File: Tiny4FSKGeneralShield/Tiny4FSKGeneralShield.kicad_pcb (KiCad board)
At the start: 4 copper layers, 27.8 x 63.9 mm, 33 parts, among them J1 Micro_SD_Card, J10 Ext.IMU, J11 Ext.Photo, J12 Int.OLED, J15 Int.Pwr, J16 3v3 IO, J17 5V IO, J2 USB_C_Receptacle_USB2.0_14P, J3 TinyI2C, J4 TinyGPIO, J5 Ext.BME280, J6 TinySPI, J7 TinyPwr, J8 TinyUSB, J9 Ext.Pwr, U1 FXMA108, U3 TPS63060

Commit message: starting to get caught up
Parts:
- C3, C4, C5, C6: footprint Capacitor_SMD:C_0805_2012Metric -> Capacitor_SMD:C_0402_1005Metric
- C7, C8, C9: footprint Capacitor_SMD:C_0805_2012Metric -> Capacitor_SMD:C_0603_1608Metric
- J1: footprint Connector_Card:microSD_HC_Hirose_DM3D-SF -> TF-PUSH:TF-PUSH
- R1, R2: value 5k1 -> 5.1kR; footprint Resistor_SMD:R_0805_2012Metric -> Resistor_SMD:R_0402_1005Metric
- R3, R5: value 1k -> 1kR; footprint Resistor_SMD:R_0805_2012Metric -> Resistor_SMD:R_0402_1005Metric
- R4, R6: value 2k -> 2kR; footprint Resistor_SMD:R_0805_2012Metric -> Resistor_SMD:R_0402_1005Metric
- R7: footprint Resistor_SMD:R_0805_2012Metric -> Resistor_SMD:R_0402_1005Metric
- R9: value 111k -> 111kR
- moved J1 26.0 mm to (174.2, 72.5)
- moved R4 2.90 mm to (141.8, 96.6)
- moved C4 2.35 mm to (151.6, 100.3), turned to 0 degrees
- moved R3 1.94 mm to (140.4, 97.0)
- moved R7 1.74 mm to (150.2, 99.9)
- moved R6 1.31 mm to (141.8, 98.6)
- moved R9 0.98 mm to (151.0, 101.8)
- moved C3 0.75 mm to (151.7, 104.0)
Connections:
- J1 pad 9: Earth -> unconnected-(J1-DET-Pad9)
- J12 pad 1: +3.3V -> SDA
- J12 pad 2: Earth -> SCL
- J12 pad 3: SCL -> +3.3V
- J12 pad 4: SDA -> Earth
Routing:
- net Earth: track 17.7 -> 10.9 mm, vias 59 -> 51
- net SCK: track 80.0 -> 74.5 mm, vias 3 -> 2
- net Net-(U3-FB): track 9.87 -> 5.76 mm
- net MOSI: track 114.6 -> 110.7 mm, vias 1 -> 0
- net MISO: track 77.3 -> 74.0 mm, vias 3 -> 2
- net A1: track 66.5 -> 69.6 mm
- net SDA: track 83.8 -> 80.9 mm, vias 0 -> 1
- net A1_5: track 20.3 -> 17.9 mm, vias 1 -> 0
- net +5V: track 79.6 -> 81.6 mm
- net +3.3V: track 5.45 -> 3.51 mm, vias 4 -> 3
- net D38: track 75.8 -> 77.3 mm
- net D12: track 49.5 -> 48.0 mm
- net SCL: track 90.9 -> 89.7 mm
- net GNDA: track 116.8 -> 115.8 mm
- net A2_5: track 18.0 -> 18.8 mm
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
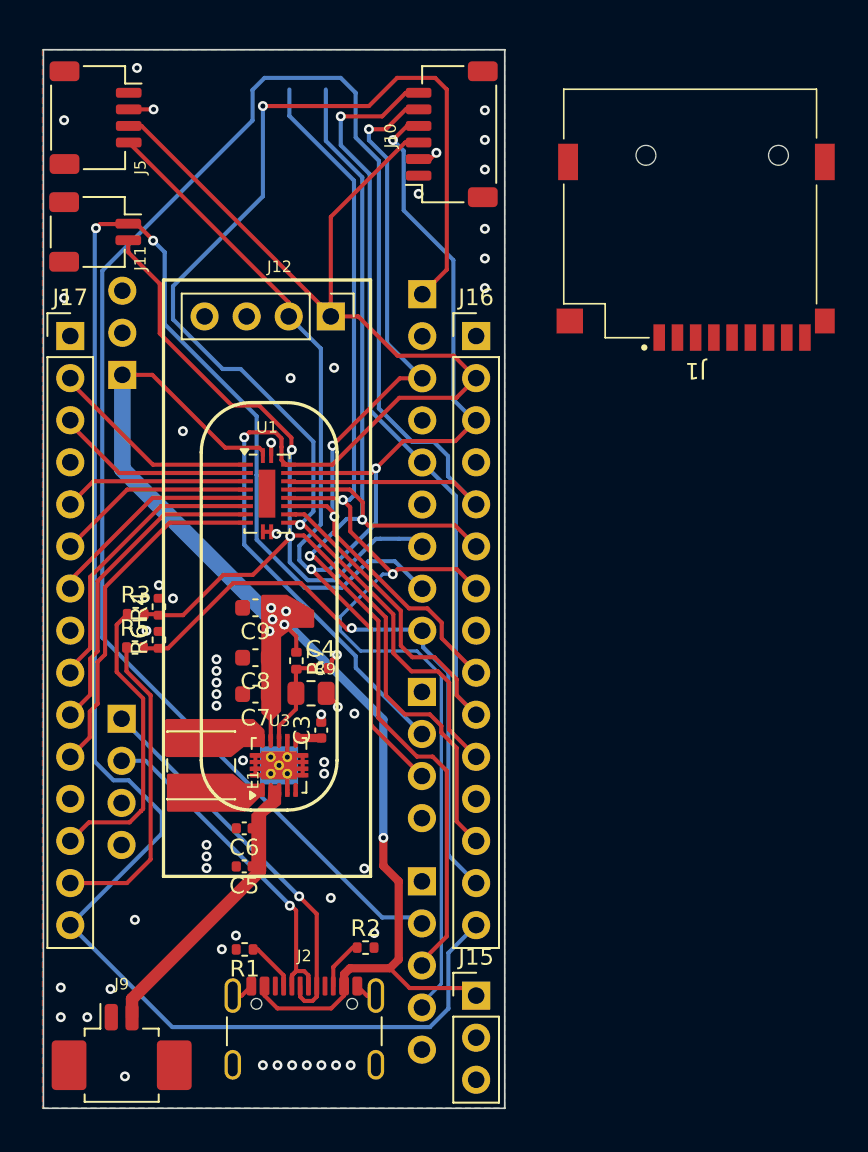
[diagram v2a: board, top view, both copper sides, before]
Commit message: need to find jlc part for qwiic
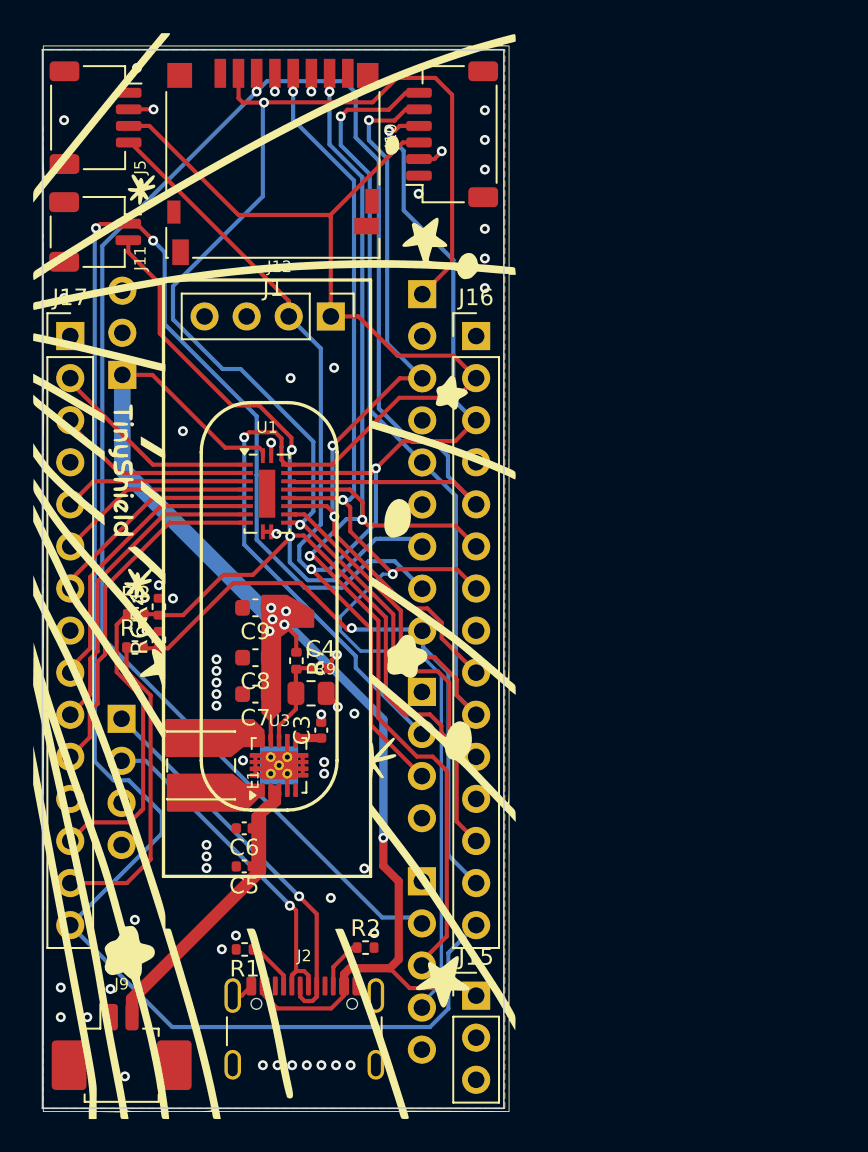
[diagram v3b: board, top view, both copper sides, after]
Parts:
- added G***: LOGO, LOGO, F.Cu at (148.8, 94.8)
- added G***: LOGO, LOGO, B.Cu at (148.8, 95.0)
- J1: footprint TF-PUSH:TF-PUSH -> Connector_Card:microSD_HC_Hirose_DM3D-SF
- moved J1 25.7 mm to (148.7, 69.8)
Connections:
- J1 pad 10: Earth -> (no net)
- J1 pad 9: unconnected-(J1-DET-Pad9) -> Earth
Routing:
- net D38: track 77.3 -> 80.8 mm
- net SDA: track 80.9 -> 78.6 mm
- net +3.3V: track 3.51 -> 4.97 mm, vias 3 -> 4
- net Earth: track 10.9 -> 12.0 mm, vias 51 -> 52
- net SCK: track 74.5 -> 75.3 mm, vias 2 -> 3
- net MISO: track 74.0 -> 74.9 mm, vias 2 -> 3
- net MOSI: track 110.7 -> 111.5 mm, vias 0 -> 1
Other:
- board size 27.8 x 63.9 mm -> 27.9 x 63.9 mm

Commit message: release candidate!
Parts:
- J9: footprint Connector_Molex:Molex_PicoBlade_53261-0271_1x02-1MP_P1.25mm_Horizontal -> Connector_JSt_Extended:HX20007-2AWB
- moved J9 3.35 mm to (140.3, 127.0), turned to 180 degrees
- moved J17 0.76 mm to (136.5, 79.5)
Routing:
- net +BATT: track 12.3 -> 17.2 mm
- net D12_5: track 17.6 -> 16.7 mm
- net SCK_5: track 13.1 -> 12.5 mm
